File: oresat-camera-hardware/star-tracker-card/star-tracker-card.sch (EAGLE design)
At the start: 316 parts, among them J1 ORESAT-DEBUG-CONNECTOR-CARD, J100 DM3BT-DSF-PEJS, J101 3-1734592-64-1734592-0, J102 FTSH-105-XX-X-DV-K, J4 TFM-120-01-L-D-RA, Q1 MMBT2907, Q2 PMV45EN, Q3 DMP2240UDM, Q4 PMV45EN, Q5 MOSFET-PCH-SOT23-6, Q6 MOSFET-PCH-SOT23-6, U1 RCLAMP0504FB, U10 TLVH431, U11 TCAN330, U12 MIC842LYC5, U13 MIC842LYC5, U14 MAX4211FETE, U15 TPS62112, U16 MAX7310ATE, U2 TPS2051CDBVR, U4 SN74LVC1G07DCK, U5 SN74LVC8T245MPWREPPW24-M, U6 CLVCH16T245MDGGREP, U7 OSD3358-512M-BSM, U8 TLV70028QDDCRQ1, U9 TCA9509DGKRDGK8-M, Y1 24MHz, Y2 ABS07-32.768KHZ-T

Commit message: implemented design review changes. Cleaned up the repo a bit. Added generic SPI EEPROM footprint for booting
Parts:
- removed J2: (no value), SparkFun-Connectors:CONN_02PTH3
- removed TP32, TP33, TP34: TEST-POINT3X4, SparkFun-Connectors:TEST-POINT3X4
- added C40: 0.1uF, oresat-rcl:C-EU0603-A
- added JP1: JUMPER-SMT_2_NO_SILK, SparkFun-Jumpers:JUMPER-SMT_2_NO_SILK
- added TP67, TP68: TEST-POINT, Tova:TEST-POINT
- added TP69: TEST-POINT3X4, SparkFun-Connectors:TEST-POINT3X4
- added U17: 25AAXX, U-Generic-SPI-EEPROM:25AAXX
- R59, R60: value 47k -> DNP; DIS Digi-Key -> (none); DPN 1276-4275-1-ND -> (none); MFR Samsung -> (none); MPN RC1005F6653CS -> (none)
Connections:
- removed net 5V_IN: C14.1, J2.2, U7A.VIN_AC@1, U7A.VIN_AC@2, U7A.VIN_AC@3
- new net N$110: R59.1, R60.2, U17.!WP
- new net N$111: TP69.1, U17.!HOLD
- new net N$112: J102.!RESET, JP1.2
- net 3.3V: now also C40.2, R60.1, U17.VCC
- net 5V: now also C14.1, U7A.VIN_AC@1, U7A.VIN_AC@2, U7A.VIN_AC@3; no longer J2.1
- net GND: now also C40.1, R59.2, U17.GND
- net N$28: now also U17.SCK; no longer TP33.1
- net N$29: now also U17.MISO; no longer TP31.1
- net N$30: now also U17.MOSI; no longer TP32.1
- net N$31: now also U17.!CS; no longer TP34.1
- net N$385: no longer R59.1, R60.1
- net N$657: now also TP31.1; no longer J102.!RESET
- net PB6/SCL: now also TP67.1; no longer R60.2
- net PB7/SDA: now also TP68.1; no longer R59.2
- net RESET#: now also JP1.1
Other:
- note added: "Pull low to program EEPROM. Program EEPROM with below script, using another Pocketbeagle oresat-star-tracker/utils/i2c-program-board-id.py"
- note added: "SPI Flash/EEPROM For SPI boot DNP for now"
- note added: "VIN_USB Provides power to the OSD335x"
- note removed: "47k forces slow I2C"
- note removed: "Place only if I2C pullups not placed."
- note removed: "Pull low to program EEPROM"
- moved on the sheet: C11, C31, C8, J100, JP102, JP103, JP110, JP111, R20, R22, R8, TP22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

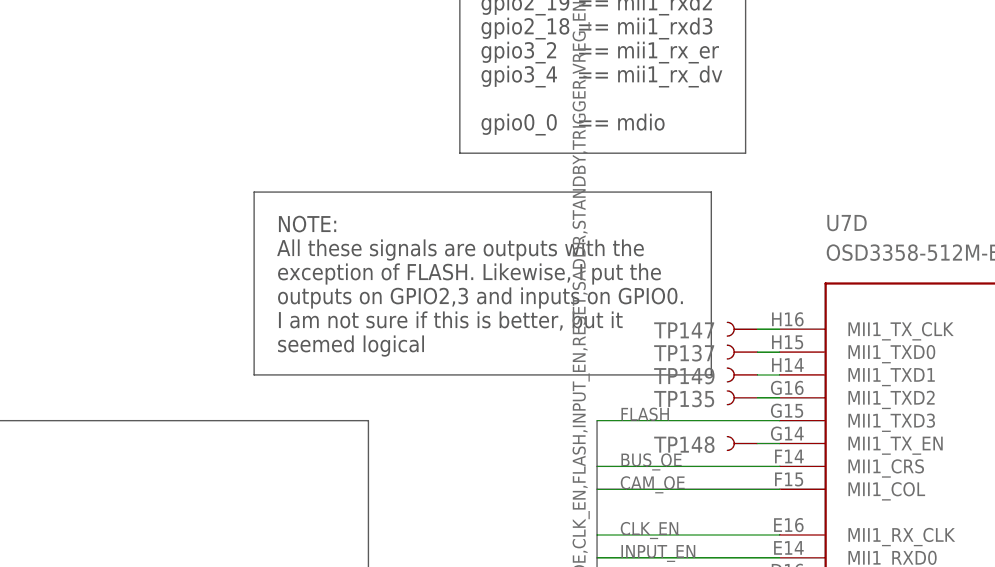
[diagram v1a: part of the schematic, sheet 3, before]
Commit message: added part number attributes
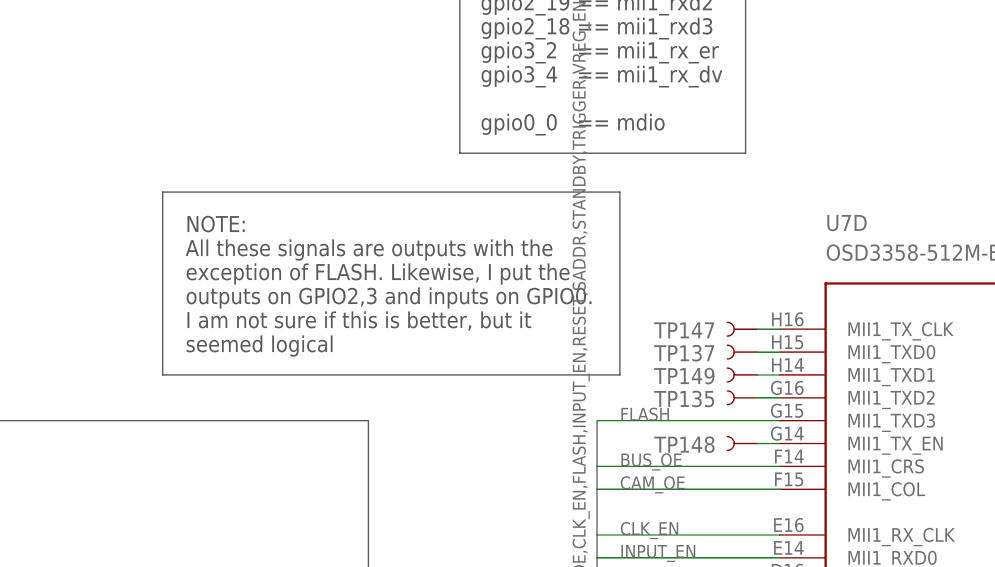
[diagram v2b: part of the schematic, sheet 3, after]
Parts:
- C18: value 0.1uF, 6.3V -> 0.1uF
- C31, C34, C37, C39, C40: DIS Digi-Key -> (none); DPN 1276-1001-1-ND -> (none); MFR Samsung -> (none); MPN CL05B104KO5NNNC -> (none)
- C32, C35: value 1u -> 1uF
- FB1, FB2: DPN (none) -> 490-14027-1-ND
- J4: MFR Samtec -> (none); MPN TFM-120-01-L-D-RA -> (none)
- L1: MFR ECS -> (none); MPN ECS-MPI4040R4-6R8-R -> (none)
- Q2, Q4: DPN (none) -> 1727-2307-1-ND; MPN (none) -> PMV45EN2R
- Q3: MFR Diodes Inc -> (none); MPN DMP2240UDM -> (none)
- Q5, Q6: MFR Diodes Inc -> (none)
- R10, R8, R9: DPN (none) -> U7103CT-ND; MPN (none) -> EXB-A10P103J
- R13: value 1M, 1% -> 1M
- R24, R25, R26: DPN (none) -> U7104CT-ND; MPN (none) -> EXB-A10P104J
- R27: value 1M, DNI -> DNP
- R28: value 10.0K -> 10k
- R32, R34, R35, R36, R37, R39, R41, R43, R44, R45, R46, R47, R48, R49, R50, R52, R61, R62, R64, R71, R72: DIS Digi-Key -> (none); DPN 1276-4275-1-ND -> (none); MFR Samsung -> (none); MPN RC1005F6653CS -> (none)
- U11: MFR Texas Instruments -> (none); MPN TCAN330GDCNT -> (none)
- U14: MFR Maxim -> (none); MPN MAX4211FETE -> (none)
- U15: MFR TI -> (none); MPN TPS62111RSA -> (none)
- U3: DPN (none) -> THGBMJG7C2LBAU8-ND; MPN (none) -> THGBMJG7C2LBAU8
- Y1: MPN ECS-240-12-30BQ-AEN-TR -> (none)
- Y2: MPN ABS07-32.768KHZ-T -> (none)
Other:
- note added: "1M if populated"

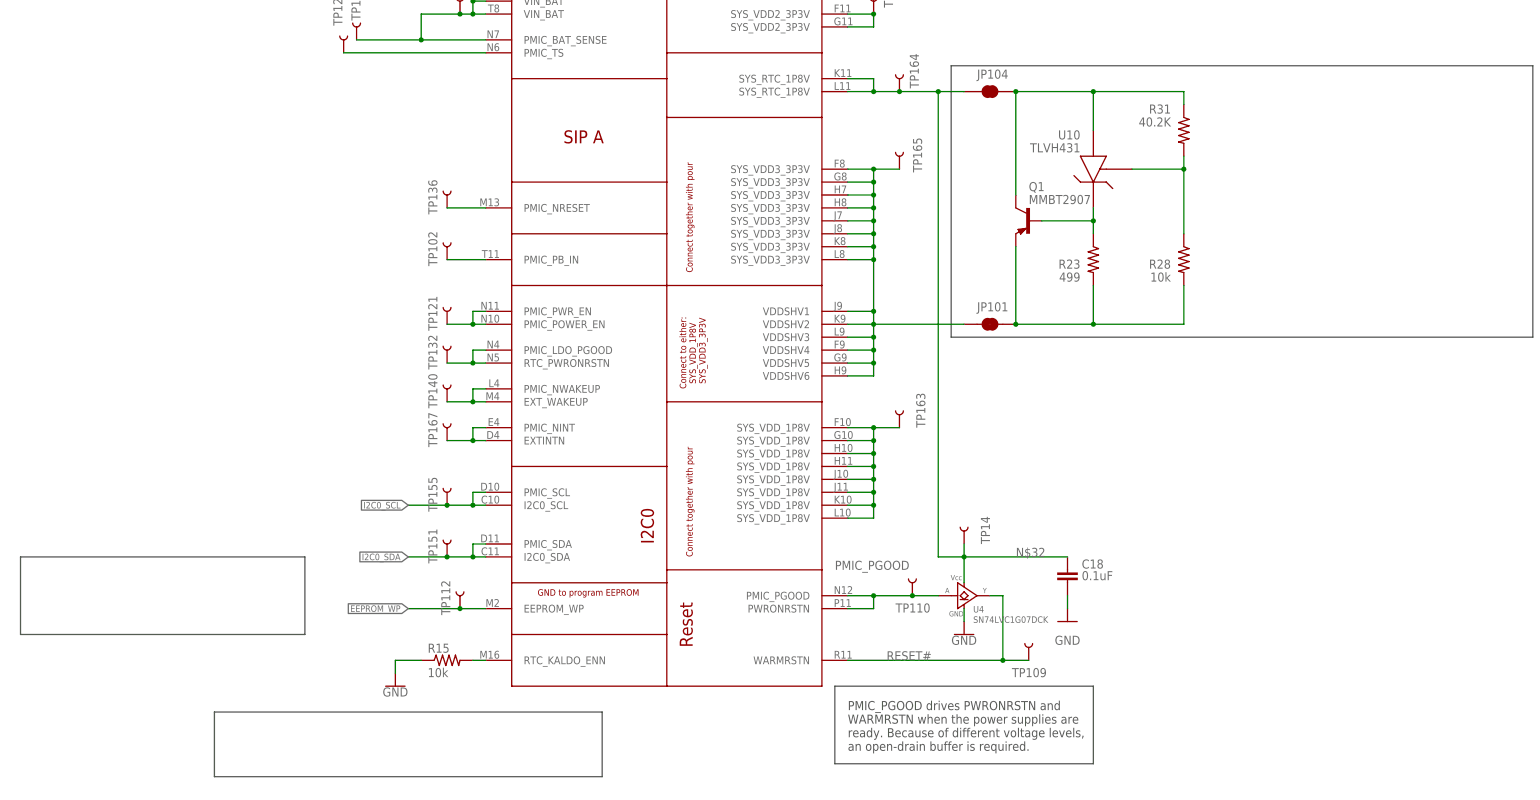
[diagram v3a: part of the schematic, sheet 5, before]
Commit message: added ESD protection to I2C0 and EEPROM_WP
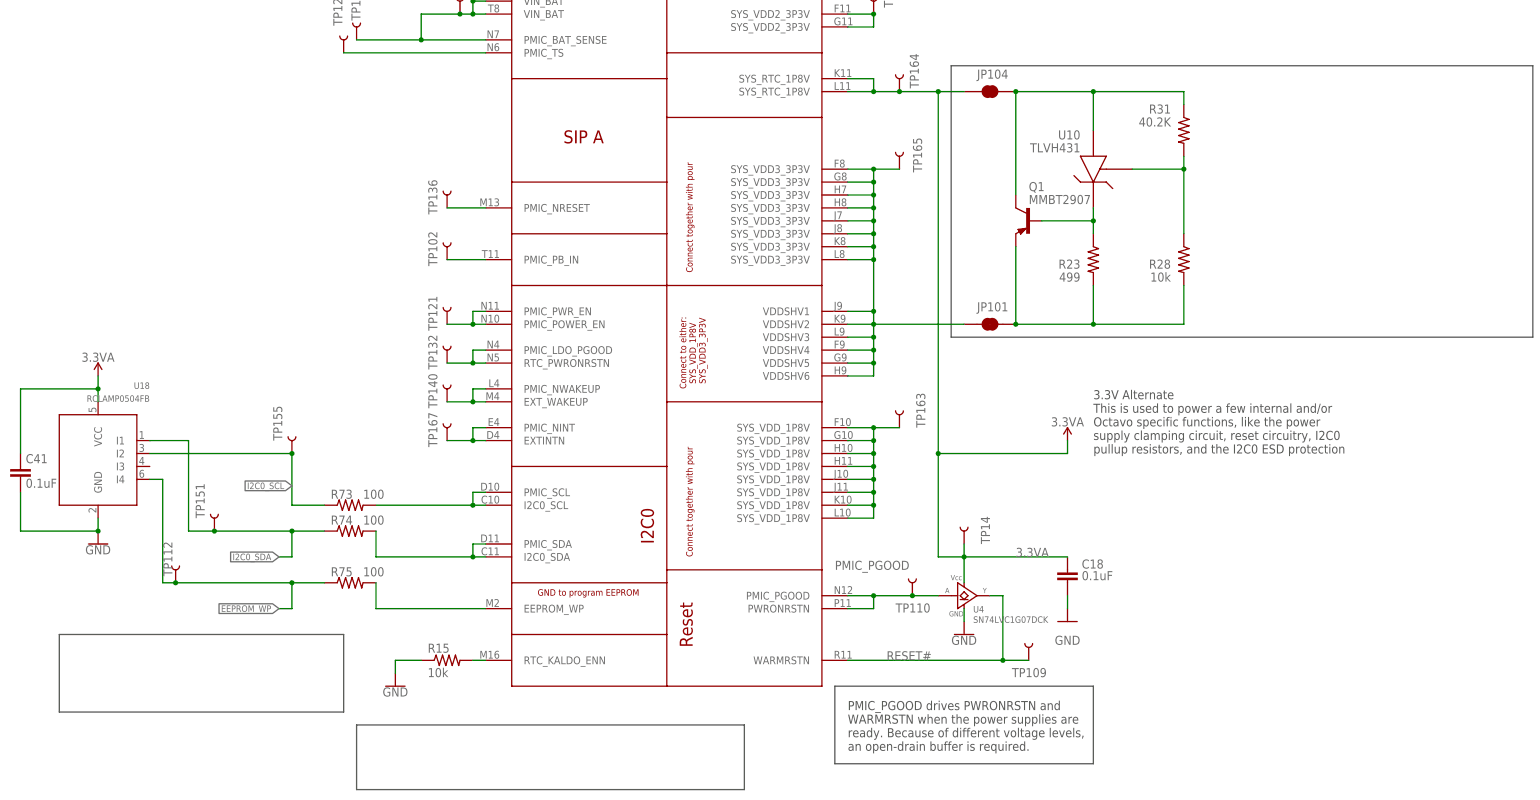
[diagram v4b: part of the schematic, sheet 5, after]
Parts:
- added C41: 0.1uF, oresat-rcl:C-EU0603-A
- added R73, R74, R75: 100, oresat-rcl:R-US_0603-A
- added U18: RCLAMP0504FB, U-Semtec-RCLAMP0504FB:RCLAMP0504FB
- JP107: value JUMPER-SMT_3_NO_NO_SILK -> JUMPER-SMT_3_NO_SILK; device SparkFun-Jumpers:JUMPER-SMT_3_NO_NO_SILK -> SparkFun-Jumpers:JUMPER-SMT_3_NO_SILK
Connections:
- removed net N$32: C18.1, JP104.1, TP14.1, TP164.1, U4.VCC, U7A.SYS_RTC_1P8V@1, U7A.SYS_RTC_1P8V@2
- new net 3.3VA: C18.1, C41.1, JP104.1, TP14.1, TP164.1, U18.VCC, U4.VCC, U7A.SYS_RTC_1P8V@1, U7A.SYS_RTC_1P8V@2
- new net N$114: R74.2, U7A.I2C0_SDA, U7A.PMIC_SDA
- new net N$115: R75.2, U7A.EEPROM_WP
- new net N$116: R73.2, U7A.I2C0_SCL, U7A.PMIC_SCL
- net EEPROM_WP: now also R75.1, U18.I4; no longer U7A.EEPROM_WP
- net GND: now also C41.2, U18.GND
- net I2C0_SCL: now also R73.1, U18.I2; no longer U7A.I2C0_SCL, U7A.PMIC_SCL
- net I2C0_SDA: now also R74.1, U18.I1; no longer U7A.I2C0_SDA, U7A.PMIC_SDA
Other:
- note added: "3.3V Alternate This is used to power a few internal and/or Octavo specific functions, like the power supply clamping circuit, reset circuitry, I2C0 pullup resistors, and the I2C0 ESD protection"
- note added: "ESD protection clamping diodes for I2C0 lines. This is required because these lines are routed externally so the internal EEPROM can be programmed."
- moved on the sheet: TP112, TP151, TP155

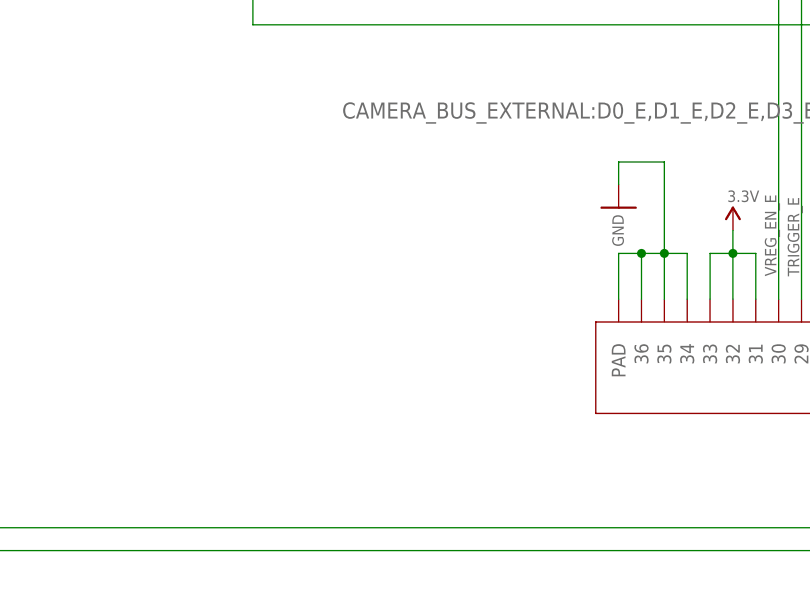
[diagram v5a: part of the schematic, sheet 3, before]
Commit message: added a couple bulk caps on 3.3v line for camera
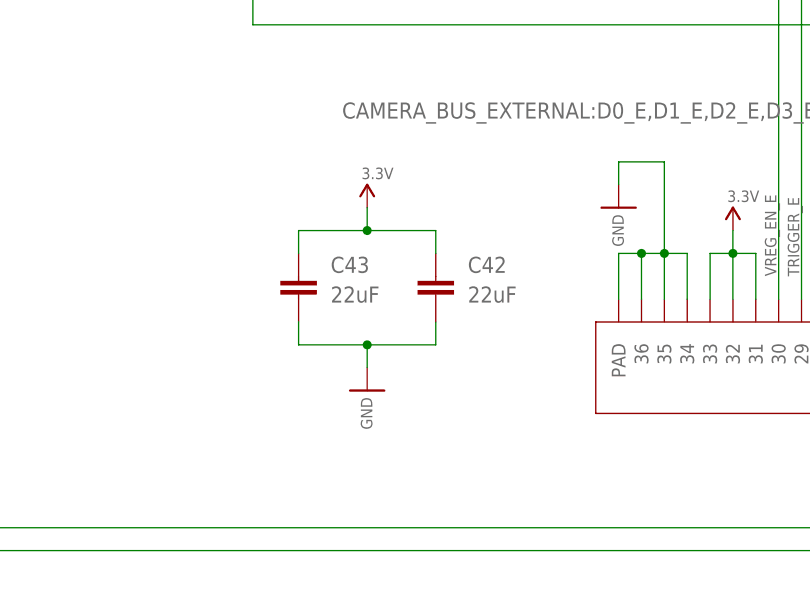
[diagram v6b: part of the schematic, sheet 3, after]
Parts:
- added C42, C43: 22uF, oresat-rcl:C-EUC1210
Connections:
- net 3.3V: now also C42.1, C43.1
- net GND: now also C42.2, C43.2
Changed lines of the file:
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@@
 <part name="R74" library="oresat-rcl" deviceset="R-US_" device="0603-A" value="100"/>
 <part name="R75" library="oresat-rcl" deviceset="R-US_" device="0603-A" value="100"/>
+<part name="C42" library="oresat-rcl" deviceset="C-EU" device="C1210" value="22uF"/>
+<part name="C43" library="oresat-rcl" deviceset="C-EU" device="C1210" value="22uF"/>
+<part name="3V-30" library="oresat-supplies" deviceset="3.3V" device=""/>
+<part name="GND55" library="SparkFun-PowerSymbols" deviceset="GND" device=""/>
 </parts>
 <sheets>
@@
 <attribute name="NAME" x="168.402" y="454.152" size="1.778" layer="95" font="vector" rot="R90"/>
 </instance>
+<instance part="C42" gate="CE" x="365.76" y="68.58" smashed="yes">
+<attribute name="NAME" x="369.316" y="68.961" size="1.778" layer="95"/>
+<attribute name="VALUE" x="369.316" y="65.659" size="1.778" layer="96"/>
+</instance>
+<instance part="C43" gate="CE" x="350.52" y="68.58" smashed="yes">
+<attribute name="NAME" x="354.076" y="68.961" size="1.778" layer="95"/>
+<attribute name="VALUE" x="354.076" y="65.659" size="1.778" layer="96"/>
+</instance>
+<instance part="3V-30" gate="G$1" x="358.14" y="78.74" smashed="yes">
+<attribute name="VALUE" x="357.505" y="79.375" size="1.27" layer="96"/>
+</instance>
+<instance part="GND55" gate="1" x="358.14" y="55.88" smashed="yes">
+<attribute name="VALUE" x="357.4415" y="53.34" size="1.27" layer="96" rot="R90" align="top-center"/>
+</instance>
 </instances>
 <busses>
@@
 <wire x1="162.56" y1="457.2" x2="162.56" y2="459.74" width="0.1524" layer="91"/>
 </segment>
+<segment>
+<pinref part="C43" gate="CE" pin="1"/>
+<wire x1="350.52" y1="71.12" x2="350.52" y2="73.66" width="0.1524" layer="91"/>
+<wire x1="350.52" y1="73.66" x2="358.14" y2="73.66" width="0.1524" layer="91"/>
+<pinref part="3V-30" gate="G$1" pin="3.3V"/>
+<wire x1="358.14" y1="73.66" x2="358.14" y2="76.2" width="0.1524" layer="91"/>
+<pinref part="C42" gate="CE" pin="1"/>
+<wire x1="365.76" y1="71.12" x2="365.76" y2="73.66" width="0.1524" layer="91"/>
+<wire x1="365.76" y1="73.66" x2="358.14" y2="73.66" width="0.1524" layer="91"/>
+<junction x="358.14" y="73.66"/>
+</segment>
 </net>
 <net name="N$535" class="0">
@@
 <wire x1="162.56" y1="436.88" x2="162.56" y2="434.34" width="0.1524" layer="91"/>
 </segment>
+<segment>
+<pinref part="C43" gate="CE" pin="2"/>
+<wire x1="350.52" y1="63.5" x2="350.52" y2="60.96" width="0.1524" layer="91"/>
+<wire x1="350.52" y1="60.96" x2="358.14" y2="60.96" width="0.1524" layer="91"/>
+<pinref part="GND55" gate="1" pin="GND"/>
+<wire x1="358.14" y1="60.96" x2="358.14" y2="58.42" width="0.1524" layer="91"/>
+<pinref part="C42" gate="CE" pin="2"/>
+<wire x1="358.14" y1="60.96" x2="365.76" y2="60.96" width="0.1524" layer="91"/>
+<wire x1="365.76" y1="60.96" x2="365.76" y2="63.5" width="0.1524" layer="91"/>
+<junction x="358.14" y="60.96"/>
+</segment>
 </net>

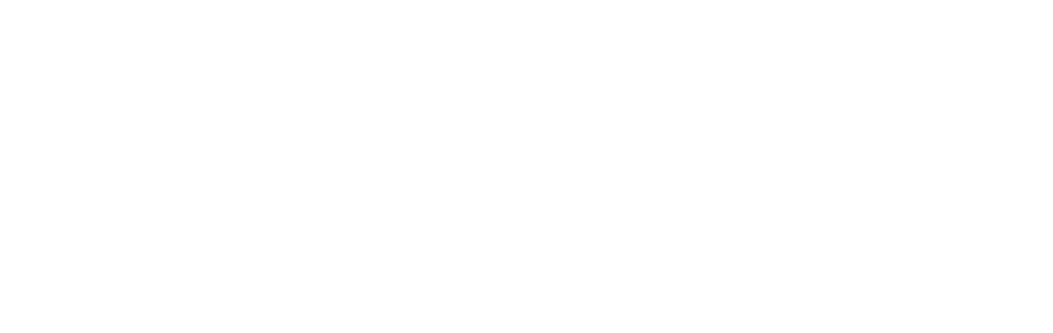
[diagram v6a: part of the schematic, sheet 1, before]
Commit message: Updated v1.2 star tracker to OreSat Cards v1.3. Shaved away an annoying 0.1 mm, added a few mm to another +X location, and cleaned up some of the TSTOP. Re-ran ERC and DRC, massaged a few things to get rid of unecessary DRCs but all super minor.
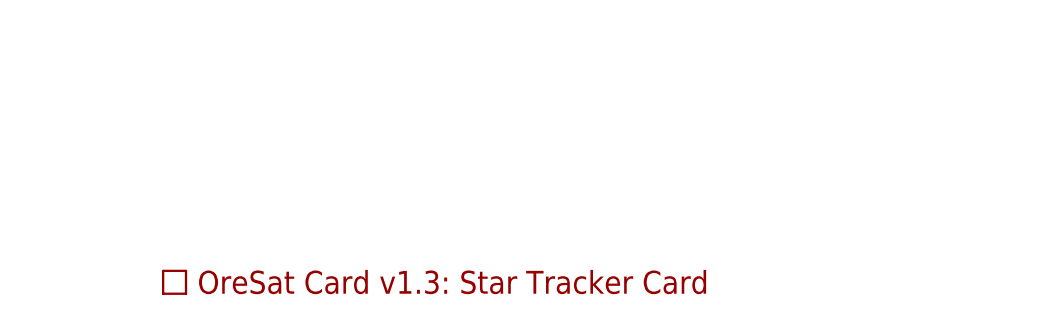
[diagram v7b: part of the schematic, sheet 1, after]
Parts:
- added PCB1: ORESAT-CARD-V1.3-STAR-TRACKER, oresat-cards:ORESAT-CARD-V1.3-STAR-TRACKER
- U3: value (none) -> THGBMJG7C2LBAU8
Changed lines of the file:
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@@
 <?xml version="1.0" encoding="utf-8"?>
 <!DOCTYPE eagle SYSTEM "eagle.dtd">
-<eagle version="9.6.2">
+<eagle version="9.6.1">
 <drawing>
 <settings>
@@
 <attribute name="MPN" value="EXB-A10P104J"/>
 </part>
-<part name="U3" library="U-Generic-eMMC-153pin" deviceset="EMMC+RESET+5.1-COMPATIBLE" device="-BA">
+<part name="U3" library="U-Generic-eMMC-153pin" deviceset="EMMC+RESET+5.1-COMPATIBLE" device="-BA" value="THGBMJG7C2LBAU8">
 <attribute name="DPN" value="THGBMJG7C2LBAU8-ND"/>
 <attribute name="MPN" value="THGBMJG7C2LBAU8"/>
@@
 <part name="3V-30" library="oresat-supplies" deviceset="3.3V" device=""/>
 <part name="GND55" library="SparkFun-PowerSymbols" deviceset="GND" device=""/>
+<part name="PCB1" library="oresat-cards" deviceset="ORESAT-CARD-V1.3-STAR-TRACKER" device=""/>
 </parts>
 <sheets>
@@
 <attribute name="VALUE" x="129.54" y="165.354" size="1.778" layer="96" align="bottom-center"/>
 </instance>
+<instance part="PCB1" gate="G$1" x="134.62" y="5.08" smashed="yes"/>
 </instances>
 <busses>
